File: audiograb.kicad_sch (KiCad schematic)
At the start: 0 parts

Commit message: add schematic for compute module
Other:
- added sheet Compute Module (compute-module.kicad_sch)
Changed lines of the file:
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@@
 		(company "NTNU, NINA")
+	)
+	(sheet
+		(at 143.51 43.18)
+		(size 43.18 33.02)
+		(exclude_from_sim no)
+		(in_bom yes)
+		(on_board yes)
+		(dnp no)
+		(fields_autoplaced yes)
+		(stroke
+			(width 0.1524)
+			(type solid)
+		)
+		(fill
+			(color 0 0 0 0.0000)
+		)
+		(property "Sheetname" "Compute Module"
+			(at 143.51 42.4684 0)
+			(effects
+				(font
+					(size 1.27 1.27)
+				)
+				(justify left bottom)
+			)
+		)
+		(property "Sheetfile" "compute-module.kicad_sch"
+			(at 143.51 76.7846 0)
+			(effects
+				(font
+					(size 1.27 1.27)
+				)
+				(justify left top)
+			)
+		)
+		(instances
+			(project "audiograb"
+				(path "/c46c2311-6d4b-411d-b012-c7730eac136d"
+					(page "2")
+				)
+			)
+		)
 	)
 	(sheet_instances

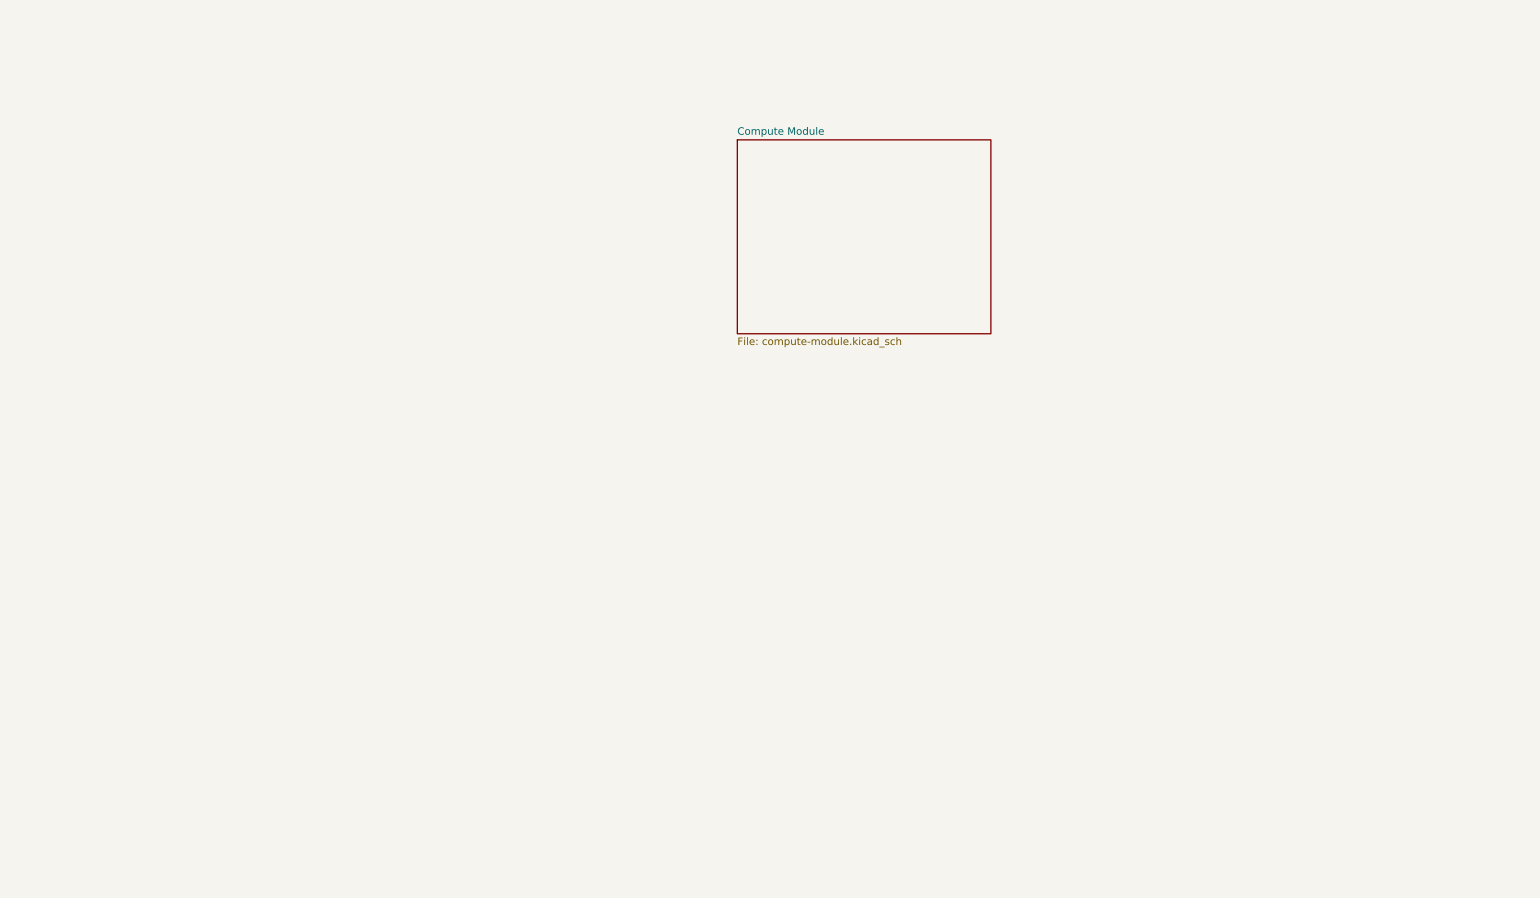
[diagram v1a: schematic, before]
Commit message: added schematics for modules
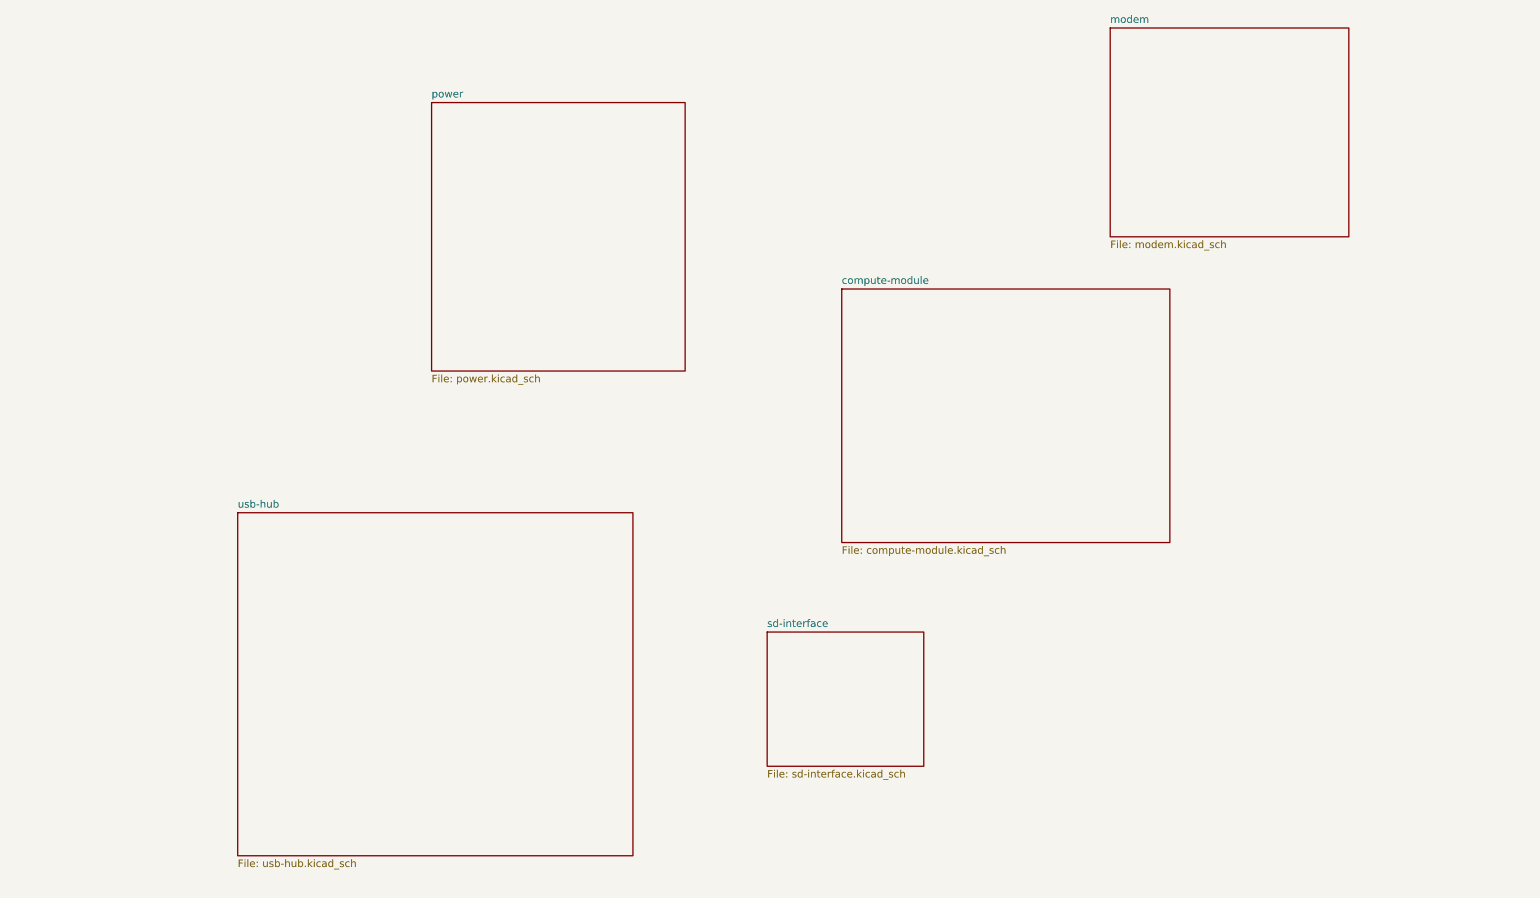
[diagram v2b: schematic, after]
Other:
- removed sheet Compute Module
- added sheet compute-module (compute-module.kicad_sch)
- added sheet modem (modem.kicad_sch)
- added sheet power (power.kicad_sch)
- added sheet sd-interface (sd-interface.kicad_sch)
- added sheet usb-hub (usb-hub.kicad_sch)
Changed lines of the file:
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@@
 	)
 	(sheet
-		(at 143.51 43.18)
-		(size 43.18 33.02)
-		(exclude_from_sim no)
-		(in_bom yes)
-		(on_board yes)
-		(dnp no)
-		(fields_autoplaced yes)
-		(stroke
-			(width 0.1524)
-			(type solid)
-		)
-		(fill
-			(color 0 0 0 0.0000)
-		)
-		(property "Sheetname" "Compute Module"
-			(at 143.51 42.4684 0)
+		(at 148.59 127)
+		(size 26.67 22.86)
+		(exclude_from_sim no)
+		(in_bom yes)
+		(on_board yes)
+		(dnp no)
+		(fields_autoplaced yes)
+		(stroke
+			(width 0.1524)
+			(type solid)
+		)
+		(fill
+			(color 0 0 0 0.0000)
+		)
+		(property "Sheetname" "sd-interface"
+			(at 148.59 126.2884 0)
+			(effects
+				(font
+					(size 1.27 1.27)
+				)
+				(justify left bottom)
+			)
+		)
+		(property "Sheetfile" "sd-interface.kicad_sch"
+			(at 148.59 150.4446 0)
+			(effects
+				(font
+					(size 1.27 1.27)
+				)
+				(justify left top)
+			)
+		)
+		(instances
+			(project "audiograb"
+				(path "/c46c2311-6d4b-411d-b012-c7730eac136d"
+					(page "5")
+				)
+			)
+		)
+	)
+	(sheet
+		(at 161.29 68.58)
+		(size 55.88 43.18)
+		(exclude_from_sim no)
+		(in_bom yes)
+		(on_board yes)
+		(dnp no)
+		(fields_autoplaced yes)
+		(stroke
+			(width 0.1524)
+			(type solid)
+		)
+		(fill
+			(color 0 0 0 0.0000)
+		)
+		(property "Sheetname" "compute-module"
+			(at 161.29 67.8684 0)
 			(effects
 				(font
@@
 		)
 		(property "Sheetfile" "compute-module.kicad_sch"
-			(at 143.51 76.7846 0)
+			(at 161.29 112.3446 0)
 			(effects
 				(font
@@
 				)
 			)
+		)
+	)
+	(sheet
+		(at 91.44 36.83)
+		(size 43.18 45.72)
+		(exclude_from_sim no)
+		(in_bom yes)
+		(on_board yes)
+		(dnp no)
+		(fields_autoplaced yes)
+		(stroke
+			(width 0.1524)
+			(type solid)
+		)
+		(fill
+			(color 0 0 0 0.0000)
+		)
+		(property "Sheetname" "power"
+			(at 91.44 36.1184 0)
+			(effects
+				(font
+					(size 1.27 1.27)
+				)
+				(justify left bottom)
+			)
+		)
+		(property "Sheetfile" "power.kicad_sch"
+			(at 91.44 83.1346 0)
+			(effects
+				(font
+					(size 1.27 1.27)
+				)
+				(justify left top)
+			)
+		)
+		(instances
+			(project "audiograb"
+				(path "/c46c2311-6d4b-411d-b012-c7730eac136d"
+					(page "3")
+				)
+			)
+		)
+	)
+	(sheet
+		(at 207.01 24.13)
+		(size 40.64 35.56)
+		(exclude_from_sim no)
+		(in_bom yes)
+		(on_board yes)
+		(dnp no)
+		(fields_autoplaced yes)
+		(stroke
+			(width 0.1524)
+			(type solid)
+		)
+		(fill
+			(color 0 0 0 0.0000)
+		)
+		(property "Sheetname" "modem"
+			(at 207.01 23.4184 0)
+			(effects
+				(font
+					(size 1.27 1.27)
+				)
+				(justify left bottom)
+			)
+		)
+		(property "Sheetfile" "modem.kicad_sch"
+			(at 207.01 60.2746 0)
+			(effects
+				(font
+					(size 1.27 1.27)
+				)
+				(justify left top)
+			)
+		)
+		(instances
+			(project "audiograb"
+				(path "/c46c2311-6d4b-411d-b012-c7730eac136d"
+					(page "6")
+				)
+			)
+		)
+	)
+	(sheet
+		(at 58.42 106.68)
+		(size 67.31 58.42)
+		(exclude_from_sim no)
+		(in_bom yes)
+		(on_board yes)
+		(dnp no)
+		(fields_autoplaced yes)
+		(stroke
+			(width 0.1524)
+			(type solid)
+		)
+		(fill
+			(color 0 0 0 0.0000)
+		)
+		(property "Sheetname" "usb-hub"
+			(at 58.42 105.9684 0)
+			(effects
+				(font
+					(size 1.27 1.27)
+				)
+				(justify left bottom)
+			)
+		)
+		(property "Sheetfile" "usb-hub.kicad_sch"
+			(at 58.42 165.6846 0)
+			(effects
+				(font
+					(size 1.27 1.27)
+				)
+				(justify left top)
+			)
+		)
+		(instances
+			(project "audiograb"
+				(path "/c46c2311-6d4b-411d-b012-c7730eac136d"
+					(page "6")
+				)
+			)

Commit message: add compute module header symbol and nets/pins
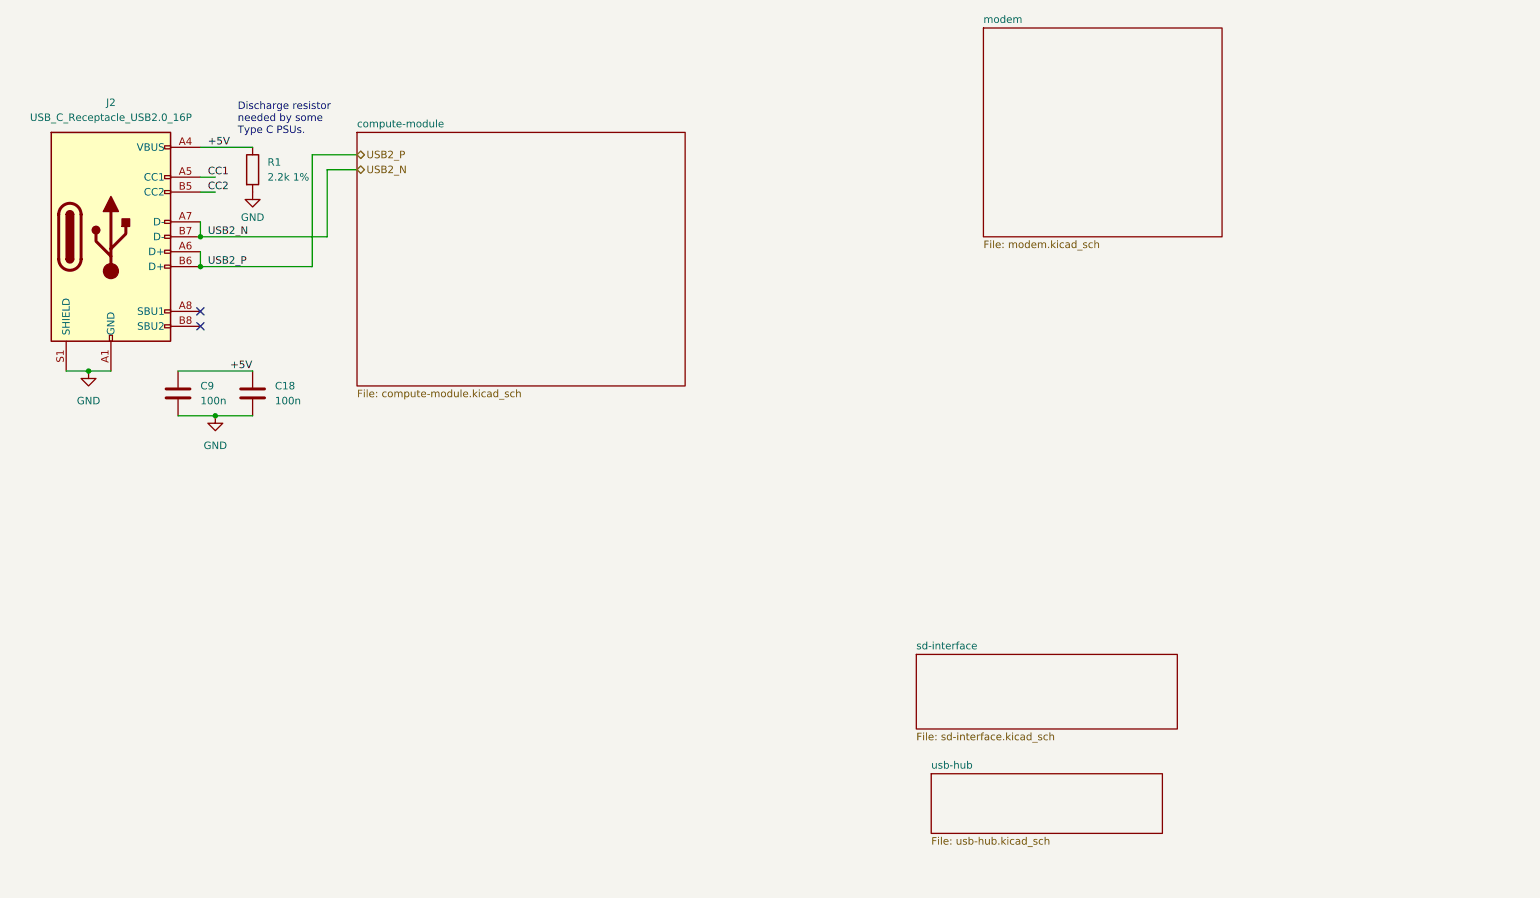
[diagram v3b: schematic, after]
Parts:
- added C18, C9: 100n, symbol Device:C
- added J2: USB_C_Receptacle_USB2.0_16P, symbol Connector:USB_C_Receptacle_USB2.0_16P
- added R1: 2.2k 1%, symbol Device:R
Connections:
- new net +5V: C18.1, C9.1, J2.A4 (VBUS), J2.A9 (VBUS), J2.B4 (VBUS), J2.B9 (VBUS), R1.1
- new net CC1: J2.A5 (CC1)
- new net CC2: J2.B5 (CC2)
- new net GND: C18.2, C9.2, J2.A1 (GND), J2.A12 (GND), J2.B1 (GND), J2.B12 (GND), J2.S1 (SHIELD), R1.2
- new net USB2_N: J2.A7 (D-), J2.B7 (D-)
- new net USB2_P: J2.A6 (D+), J2.B6 (D+)
- no-connect marks 0 -> 2
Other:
- removed sheet power
- note added: "Discharge resistor needed by some Type C PSUs."

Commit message: organise subschematics into sch/
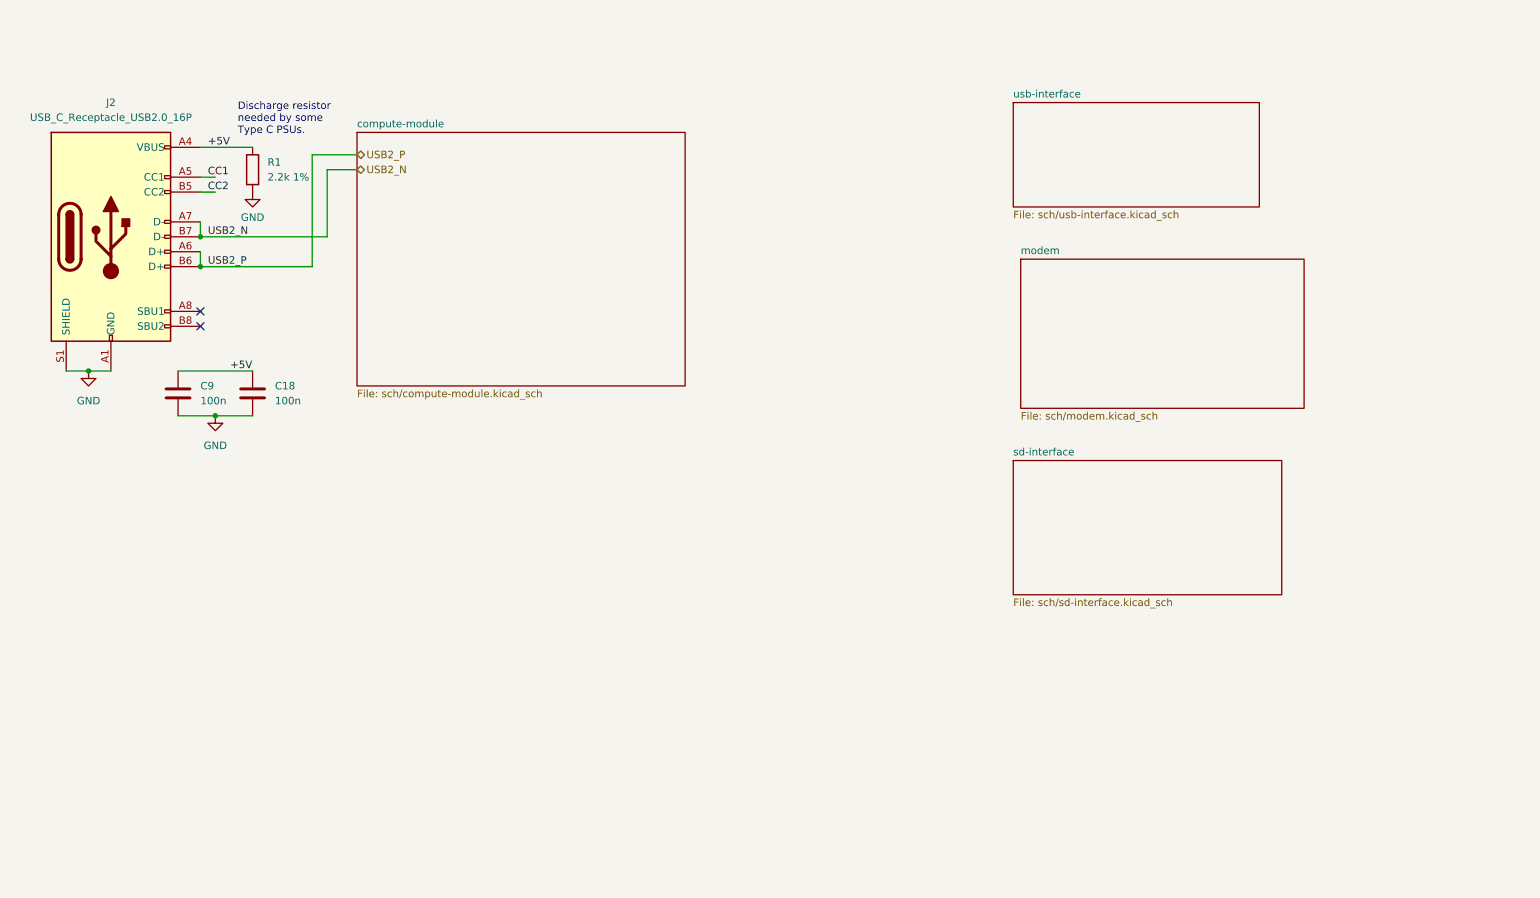
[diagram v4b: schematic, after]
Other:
- removed sheet usb-hub
- added sheet usb-interface (sch/usb-interface.kicad_sch)
- sheet compute-module: file compute-module.kicad_sch -> sch/compute-module.kicad_sch
- sheet modem: file modem.kicad_sch -> sch/modem.kicad_sch
- sheet sd-interface: file sd-interface.kicad_sch -> sch/sd-interface.kicad_sch
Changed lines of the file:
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@@
 	)
 	(sheet
-		(at 173.99 130.81)
-		(size 44.45 12.7)
+		(at 191.77 63.5)
+		(size 48.26 25.4)
+		(exclude_from_sim no)
+		(in_bom yes)
+		(on_board yes)
+		(dnp no)
+		(fields_autoplaced yes)
+		(stroke
+			(width 0.1524)
+			(type solid)
+		)
+		(fill
+			(color 0 0 0 0.0000)
+		)
+		(property "Sheetname" "modem"
+			(at 191.77 62.7884 0)
+			(effects
+				(font
+					(size 1.27 1.27)
+				)
+				(justify left bottom)
+			)
+		)
+		(property "Sheetfile" "sch/modem.kicad_sch"
+			(at 191.77 89.4846 0)
+			(effects
+				(font
+					(size 1.27 1.27)
+				)
+				(justify left top)
+			)
+		)
+		(instances
+			(project "audiograb"
+				(path "/c46c2311-6d4b-411d-b012-c7730eac136d"
+					(page "3")
+				)
+			)
+		)
+	)
+	(sheet
+		(at 190.5 36.83)
+		(size 41.91 17.78)
+		(exclude_from_sim no)
+		(in_bom yes)
+		(on_board yes)
+		(dnp no)
+		(fields_autoplaced yes)
+		(stroke
+			(width 0.1524)
+			(type solid)
+		)
+		(fill
+			(color 0 0 0 0.0000)
+		)
+		(property "Sheetname" "usb-interface"
+			(at 190.5 36.1184 0)
+			(effects
+				(font
+					(size 1.27 1.27)
+				)
+				(justify left bottom)
+			)
+		)
+		(property "Sheetfile" "sch/usb-interface.kicad_sch"
+			(at 190.5 55.1946 0)
+			(effects
+				(font
+					(size 1.27 1.27)
+				)
+				(justify left top)
+			)
+		)
+		(instances
+			(project "audiograb"
+				(path "/c46c2311-6d4b-411d-b012-c7730eac136d"
+					(page "5")
+				)
+			)
+		)
+	)
+	(sheet
+		(at 190.5 97.79)
+		(size 45.72 22.86)
 		(exclude_from_sim no)
 		(in_bom yes)
@@
 		)
 		(property "Sheetname" "sd-interface"
-			(at 173.99 130.0984 0)
+			(at 190.5 97.0784 0)
 			(effects
 				(font
@@
 			)
 		)
-		(property "Sheetfile" "sd-interface.kicad_sch"
-			(at 173.99 144.0946 0)
+		(property "Sheetfile" "sch/sd-interface.kicad_sch"
+			(at 190.5 121.2346 0)
 			(effects
 				(font
@@
 			(project "audiograb"
 				(path "/c46c2311-6d4b-411d-b012-c7730eac136d"
-					(page "5")
+					(page "4")
 				)
 			)
@@
 			)
 		)
-		(property "Sheetfile" "compute-module.kicad_sch"
+		(property "Sheetfile" "sch/compute-module.kicad_sch"
 			(at 78.74 85.6746 0)
 			(effects
@@
 				)
 			)
-		)
-	)
-	(sheet
-		(at 185.42 24.13)
-		(size 40.64 35.56)
-		(exclude_from_sim no)
-		(in_bom yes)
-		(on_board yes)
-		(dnp no)
-		(fields_autoplaced yes)
-		(stroke
-			(width 0.1524)
-			(type solid)
-		)
-		(fill
-			(color 0 0 0 0.0000)
-		)
-		(property "Sheetname" "modem"
-			(at 185.42 23.4184 0)
-			(effects
-				(font
-					(size 1.27 1.27)
-				)
-				(justify left bottom)
-			)
-		)
-		(property "Sheetfile" "modem.kicad_sch"
-			(at 185.42 60.2746 0)
-			(effects
-				(font
-					(size 1.27 1.27)
-				)
-				(justify left top)
-			)
-		)
-		(instances
-			(project "audiograb"
-				(path "/c46c2311-6d4b-411d-b012-c7730eac136d"
-					(page "6")
-				)
-			)
-		)
-	)
-	(sheet
-		(at 176.53 151.13)
-		(size 39.37 10.16)
-		(exclude_from_sim no)
-		(in_bom yes)
-		(on_board yes)
-		(dnp no)
-		(fields_autoplaced yes)
-		(stroke
-			(width 0.1524)
-			(type solid)
-		)
-		(fill
-			(color 0 0 0 0.0000)
-		)
-		(property "Sheetname" "usb-hub"
-			(at 176.53 150.4184 0)
-			(effects
-				(font
-					(size 1.27 1.27)
-				)
-				(justify left bottom)
-			)
-		)
-		(property "Sheetfile" "usb-hub.kicad_sch"
-			(at 176.53 161.8746 0)
-			(effects
-				(font
-					(size 1.27 1.27)
-				)
-				(justify left top)
-			)
-		)
-		(instances
-			(project "audiograb"
-				(path "/c46c2311-6d4b-411d-b012-c7730eac136d"
-					(page "6")
-				)
-			)
